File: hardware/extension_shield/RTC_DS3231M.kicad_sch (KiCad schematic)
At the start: 8 parts, among them U1 DS3231M

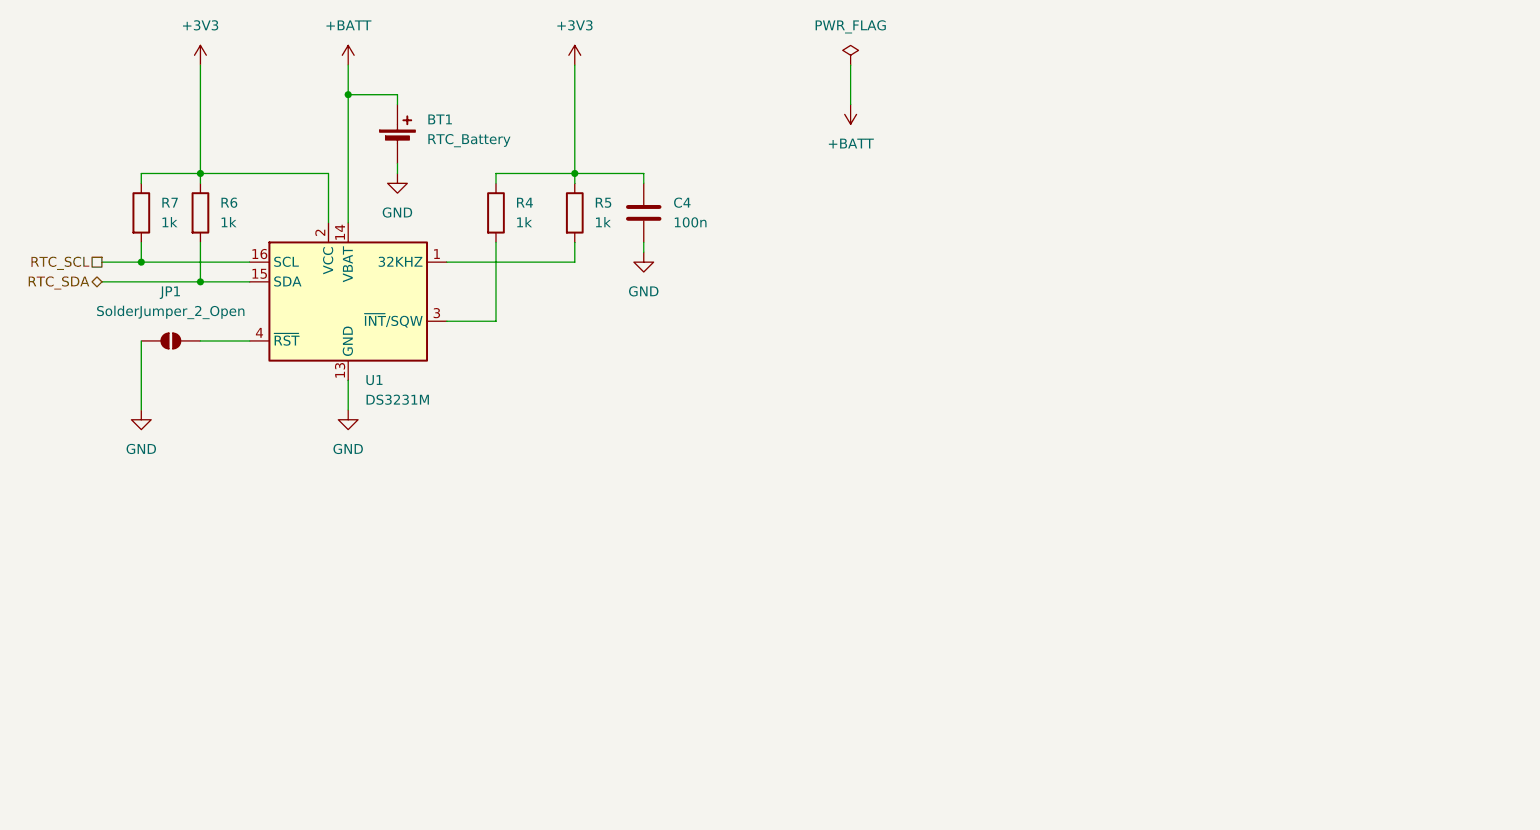
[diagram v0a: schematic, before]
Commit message: [HW] Adds Labels To Expansion Shield Schematic, PDF Schematic & Performed Schematic, PCB Tests.
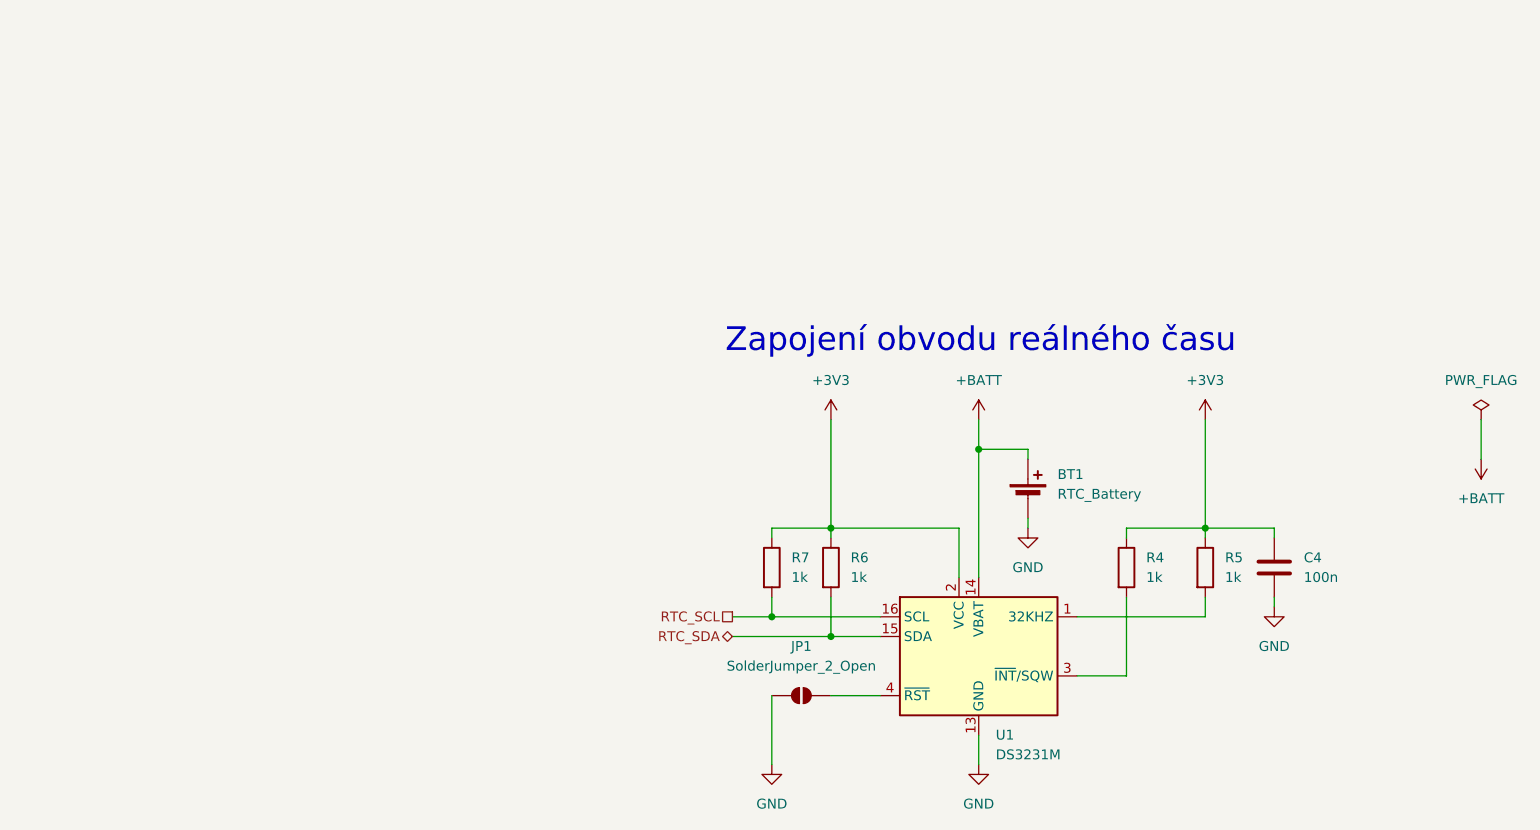
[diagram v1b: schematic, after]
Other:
- note added: "Zapojení obvodu reálného času"
- title: Datalogger Expansion Shield -> Data Logger Expansion Shield
- moved on the sheet: BT1, C4, JP1, R4, R5, R6, R7, U1
